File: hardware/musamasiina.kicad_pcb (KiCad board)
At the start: 2 copper layers, 50 x 45 mm, 73 parts, among them U2 MIC5233-3.3, U3 LTC6257, U4 TPS22860

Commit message: Start placement of parts
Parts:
- added C19: 470u, footprints:C_Radial_D6.3_L13_P2-5_Bent, F.Cu at (142.2, 56.5)
- added C20: 470u, footprints:C_Radial_D6.3_L13_P2-5_Bent, F.Cu at (142.2, 63.2)
- added C21: 470u, footprints:C_Radial_D6.3_L13_P2-5_Bent, F.Cu at (142.2, 70.0)
- added C4: AFK477M10F24T-F, footprints:C_Radial_D6.3_L13_P2-5_Bent, F.Cu at (142.2, 76.8)
- added P1: USB_OTG, Connect:USB_Micro-B_10103594-0001LF, F.Cu at (155.0, 90.0)
- added P2: CONN_02X05, Pin_Headers:Pin_Header_Straight_2x05_Pitch1.27mm, F.Cu at (131.2, 87.8)
- added P3: CONN_02X03, Pin_Headers:Pin_Header_Straight_2x03, F.Cu at (135.5, 98.0)
- added P4: CONN_01X06, Pin_Headers:Pin_Header_Straight_1x06, F.Cu at (145.0, 98.0)
- added U1: WT32, footprints:WT32, F.Cu at (123.0, 75.0)
- D1: footprint footprints:SMD0805-CAP-M -> footprints:SOD323-M
- U2: footprint footprints:SOT23-5-M -> footprints:SOT23-6-M
- U4: footprint footprints:SOT23-6-M -> footprints:SOT23-5-M
- moved D11 88.1 mm to (149.2, 58.0), turned to 180 degrees
- moved R23 87.1 mm to (149.2, 85.8), turned to 180 degrees
- moved R24 85.3 mm to (146.2, 79.6)
- moved FB11 85.3 mm to (156.0, 60.5)
- moved FB9 82.9 mm to (156.0, 57.0)
- moved FB2 82.8 mm to (149.2, 88.2), turned to 180 degrees
- moved C26 81.6 mm to (152.5, 58.0), turned to 270 degrees
- moved C27 79.5 mm to (152.5, 63.0), turned to 90 degrees
- moved FB10 79.1 mm to (156.0, 63.8)
- moved D12 78.4 mm to (149.2, 62.8)
- moved D5 72.5 mm to (145.5, 90.2), turned to 90 degrees
- moved R14 72.5 mm to (155.3, 115.4)
- moved D1 71.3 mm to (70.9, 139.2)
- moved FB1 67.8 mm to (149.2, 92.8), turned to 180 degrees
- moved C13 66.7 mm to (144.8, 94.5), turned to 180 degrees
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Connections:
- R6 pad 2: /USB_DN -> /USB_D-
- R7 pad 2: /USB_DP -> /USB_D+
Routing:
- net /USB_D-: track 0.00 -> 29.0 mm
- net /USB_D+: track 0.00 -> 28.3 mm
- net Net-(R7-Pad1): track 0.00 -> 3.17 mm
- net Net-(R6-Pad1): track 0.00 -> 3.17 mm
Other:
- board size 50 x 45 mm -> 50 x 50 mm
- net class Default: clearance 0.2 -> 0.15; via_dia 0.6 -> 0.7; via_drill 0.4 -> 0.3
- net class USB_DATA added: clearance 0.15, trace_width 0.225, via_dia 0.7, via_drill 0.3
- rule trace_clearance: 0.2 -> 0.15
- rule via_min_size: 0.4 -> 0.6

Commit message: Continue placing parts
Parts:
- added P5: CONN_01X03, footprints:SMD_3-5mm_jack_CUI-SJ-352X-SMT, B.Cu at (160.0, 59.0)
- added P6: CONN_01X03, footprints:SMD_3-5mm_jack_CUI-SJ-352X-SMT, B.Cu at (160.0, 69.2)
- added P7: CONN_01X03, footprints:SMD_3-5mm_jack_CUI-SJ-352X-SMT, B.Cu at (160.0, 79.5)
- C19, C20, C21, C4: moved to B.Cu
- moved C2 92.9 mm to (118.2, 48.5)
- moved C11 92.0 mm to (141.5, 88.5)
- moved C18 82.5 mm to (123.0, 53.0), turned to 180 degrees
- moved C14 81.7 mm to (117.2, 56.2), turned to 90 degrees
- moved R9 80.3 mm to (114.8, 56.2), turned to 270 degrees
- moved C16 77.0 mm to (125.2, 61.0)
- moved R16 76.7 mm to (133.8, 56.2), turned to 90 degrees
- moved R10 75.0 mm to (112.2, 56.2), turned to 90 degrees
- moved R15 73.0 mm to (131.2, 56.2), turned to 90 degrees
- moved R11 71.8 mm to (112.2, 60.8), turned to 270 degrees
- moved C15 71.7 mm to (120.8, 61.0)
- moved R21 70.8 mm to (128.8, 60.8), turned to 90 degrees
- moved R13 70.6 mm to (131.2, 60.8), turned to 270 degrees
- moved D4 70.4 mm to (123.9, 111.4)
- moved C3 70.3 mm to (123.0, 48.5)
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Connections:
- C7 pad 1: /Line in/ESD+ -> VAA
- C8 pad 1: /Line in/ESD+ -> VAA
- D10 pad 2: /Line in/ESD+ -> VAA
- D11 pad 2: /Line in/ESD+ -> VAA
- D12 pad 2: /Line in/ESD+ -> VAA
- D9 pad 2: /Line in/ESD+ -> VAA
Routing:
- net VCC: track 0.00 -> 1.50 mm, vias 0 -> 1
- net /IN_RIGHT: track 0.00 -> 1.50 mm, vias 0 -> 1
- net /IN_LEFT: track 0.00 -> 1.50 mm, vias 0 -> 1
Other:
- outline, holes or cut-outs redrawn

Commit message: Adjust layout
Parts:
- moved R18 58.8 mm to (107.4, 58.9)
- moved R19 43.1 mm to (136.2, 60.8), turned to 270 degrees
- moved P2 33.1 mm to (96.0, 78.0)
- moved R4 9.96 mm to (101.0, 84.0)
- moved D3 6.93 mm to (101.0, 86.0)
- moved FB1 2.26 mm to (149.5, 95.0)
- moved P1 2.00 mm to (155.0, 92.0)
- turned C15 to 180 degrees
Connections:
- net /Analog/N_LEFT renamed /Analog/LO_N
- net /Analog/N_RIGHT renamed /Analog/RO_N
- net /Analog/P_LEFT renamed /Analog/LO_P
- net /Analog/P_RIGHT renamed /Analog/RO_P
- net Net-(C15-Pad2) renamed /Analog/LEFT_OPAMP-
- net Net-(C16-Pad2) renamed /Analog/RIGHT_OPAMP-
- net Net-(R11-Pad1) renamed /Analog/LEFT_OPAMP+
- net Net-(R13-Pad1) renamed /Analog/RIGHT_OPAMP+
- net Net-(R6-Pad1) renamed /CD-
- net Net-(R7-Pad1) renamed /CD+
- C15 pad 1: Net-(C15-Pad1) -> /Analog/LEFT_SE
- C16 pad 1: Net-(C16-Pad1) -> /Analog/RIGHT_SE
- C19 pad 2: Net-(C15-Pad1) -> /Analog/LEFT_SE
- C20 pad 2: Net-(C16-Pad1) -> /Analog/RIGHT_SE
- R15 pad 2: /Stereo out/LEFT_DEVICE -> /Analog/LEFT_SE
- R16 pad 2: /Stereo out/RIGHT_DEVICE -> /Analog/RIGHT_SE
- R20 pad 1: Net-(C15-Pad1) -> /Analog/LEFT_SE
- R21 pad 1: Net-(C16-Pad1) -> /Analog/RIGHT_SE
- U3 pad 10: Net-(C16-Pad1) -> /Analog/RIGHT_SE
- U3 pad 7: Net-(C15-Pad1) -> /Analog/LEFT_SE
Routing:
- net /USB_D-: track 29.0 -> 0.00 mm
- net /USB_D+: track 28.3 -> 0.00 mm
- net /Analog/RO_P: track 0.00 -> 20.2 mm
- net /Analog/RO_N: track 0.00 -> 20.2 mm
- net /Analog/RIGHT_OPAMP-: track 0.00 -> 15.3 mm
- net /Analog/LEFT_OPAMP-: track 0.00 -> 14.1 mm
- net /Analog/LEFT_OPAMP+: track 0.00 -> 10.2 mm
- net /Analog/RIGHT_SE: track 0.00 -> 9.78 mm
- net /Analog/LEFT_SE: track 0.00 -> 9.77 mm
- net Net-(C14-Pad1): track 0.00 -> 9.43 mm
- net /Analog/RIGHT_OPAMP+: track 0.00 -> 7.57 mm
- net /Analog/LO_N: track 0.00 -> 6.50 mm
- net /Analog/LO_P: track 0.00 -> 5.93 mm
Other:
- net class Default: clearance 0.15 -> 0.2
- net class Opamp_differential added: clearance 0.15, trace_width 0.2, via_dia 0.7, via_drill 0.3
- rule trace_clearance: 0.15 -> 0.2

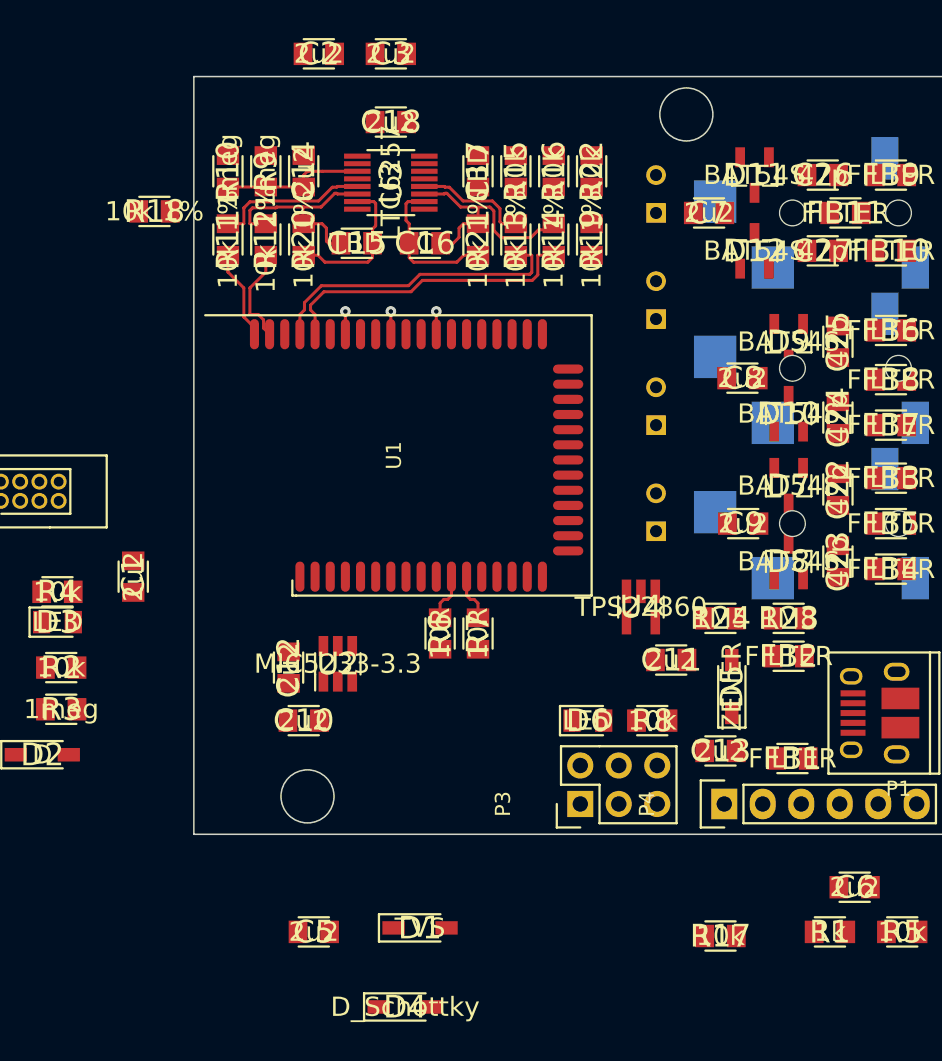
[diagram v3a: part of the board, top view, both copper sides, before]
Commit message: Add KiCAD footprints to project folder
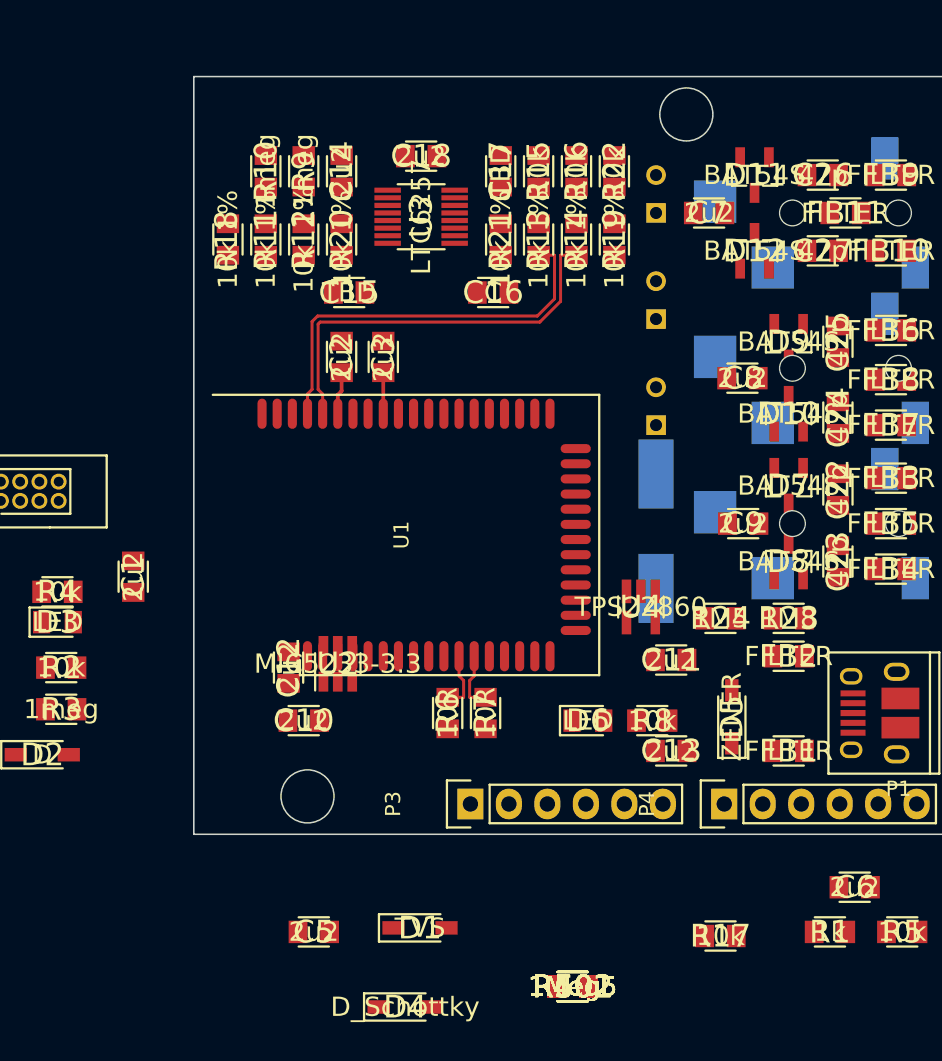
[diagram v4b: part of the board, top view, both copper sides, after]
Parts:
- added R401, R402, R501, R502, R601, R602: 1Meg5, footprints:SMD0805-RES-M, F.Cu at (135.0, 110.1)
- C4: footprint footprints:C_Radial_D6.3_L13_P2-5_Bent -> footprints:SMD_ELEC_8mmdia-M
- P3: footprint Pin_Headers:Pin_Header_Straight_2x03 -> kicad_lib:Pin_Header_Straight_1x06
- P4: footprint Pin_Headers:Pin_Header_Straight_1x06 -> kicad_lib:Pin_Header_Straight_1x06
- moved C2 20.1 mm to (119.8, 68.5), turned to 270 degrees
- moved C3 20.0 mm to (122.5, 68.5), turned to 270 degrees
- moved P3 7.25 mm to (128.2, 98.0)
- moved C16 5.55 mm to (129.8, 64.2), turned to 180 degrees
- moved R6 5.27 mm to (126.8, 92.0)
- moved R7 5.27 mm to (129.2, 92.0)
- moved U1 5.27 mm to (123.5, 80.2)
- moved R18 5.19 mm to (112.2, 60.8), turned to 270 degrees
- moved C15 3.29 mm to (120.2, 64.2), turned to 0 degrees
- moved C13 3.25 mm to (141.5, 94.5)
- moved C18 3.01 mm to (125.0, 55.2)
- moved U3 3.01 mm to (125.0, 59.2)
- moved C14 2.50 mm to (119.8, 56.2)
- moved R10 2.50 mm to (114.8, 56.2)
- moved R11 2.50 mm to (114.8, 60.8)
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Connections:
- P1 pad 4: Net-(P1-Pad4) -> /Power Supply/GNDBUS
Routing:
- net /Analog/RIGHT_OPAMP-: track 15.3 -> 0.00 mm
- net /Analog/LEFT_OPAMP-: track 14.1 -> 0.00 mm
- net /Analog/LEFT_OPAMP+: track 10.2 -> 0.00 mm
- net /Analog/RIGHT_SE: track 9.78 -> 0.00 mm
- net /Analog/LEFT_SE: track 9.77 -> 0.00 mm
- net Net-(C14-Pad1): track 9.43 -> 0.00 mm
- net /Analog/RIGHT_OPAMP+: track 7.57 -> 0.00 mm
- net /Analog/RO_N: track 20.2 -> 26.8 mm
- net /Analog/RO_P: track 20.2 -> 26.8 mm
- net /Analog/LO_N: track 6.50 -> 0.00 mm
- net /Analog/LO_P: track 5.93 -> 0.00 mm
- net Net-(C2-Pad2): track 0.00 -> 2.81 mm
- net Net-(C3-Pad2): track 0.00 -> 2.71 mm
- net VCC: track 1.50 -> 0.00 mm, vias 1 -> 0
- net /IN_RIGHT: track 1.50 -> 0.00 mm, vias 1 -> 0
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
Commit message: Update layout
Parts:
- removed R401, R402, R501, R502, R601, R602: 1Meg5, footprints:SMD0805-RES-M
- added C28: 2u2, footprints:SMD0805-CAP-M, F.Cu at (142.8, 82.8)
- added R25: 1Meg5, footprints:SMD0805-RES-M, F.Cu at (143.8, 76.0)
- added R26: 1Meg5, footprints:SMD0805-RES-M, F.Cu at (151.5, 74.2)
- added R27: 1Meg5, footprints:SMD0805-RES-M, F.Cu at (151.5, 64.0)
- added R28: 1Meg5, footprints:SMD0805-RES-M, F.Cu at (156.0, 74.2)
- added R29: 1Meg5, footprints:SMD0805-RES-M, F.Cu at (156.0, 64.0)
- added R30: 1Meg5, footprints:SMD0805-RES-M, F.Cu at (143.0, 62.5)
- C4: footprint footprints:SMD_ELEC_8mmdia-M -> footprints:C_Radial_D6.3_L13_P2-5_Bent
- P2: moved to B.Cu
- P4: footprint kicad_lib:Pin_Header_Straight_1x06 -> Pin_Headers:Pin_Header_Straight_1x06
- moved R17 54.5 mm to (126.7, 55.2)
- moved R1 44.4 mm to (132.5, 66.5)
- moved C6 43.7 mm to (127.5, 68.5), turned to 270 degrees
- moved D2 42.8 mm to (137.2, 73.8), turned to 270 degrees
- moved R2 40.6 mm to (136.0, 68.0), turned to 90 degrees
- moved C5 38.6 mm to (125.0, 68.5), turned to 270 degrees
- moved D1 37.6 mm to (131.8, 69.2)
- moved D4 34.3 mm to (137.2, 79.8), turned to 90 degrees
- moved R4 24.2 mm to (123.2, 93.5)
- moved D3 22.8 mm to (123.2, 91.0)
- moved R5 21.2 mm to (142.0, 91.2), turned to 180 degrees
- moved C10 21.0 mm to (138.2, 92.2), turned to 270 degrees
- moved R3 18.5 mm to (119.8, 92.0), turned to 270 degrees
- moved P2 18.5 mm to (112.2, 69.2), turned to 0 degrees
- moved U2 15.9 mm to (135.0, 92.2), turned to 180 degrees
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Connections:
- C11 pad 2: GNDA -> GNDD
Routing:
- net /USB_D+: track 0.00 -> 30.9 mm
- net /USB_D-: track 0.00 -> 30.9 mm
- net /Analog/LEFT_OPAMP-: track 0.00 -> 15.8 mm
- net /Analog/RIGHT_OPAMP+: track 0.00 -> 14.2 mm
- net Net-(C14-Pad1): track 0.00 -> 13.3 mm
- net /Analog/LO_P: track 0.00 -> 13.2 mm
- net /Analog/LO_N: track 0.00 -> 13.0 mm
- net /Analog/RIGHT_OPAMP-: track 0.00 -> 12.5 mm
- net /Analog/LEFT_OPAMP+: track 0.00 -> 9.48 mm
- net /Analog/LEFT_SE: track 0.00 -> 6.47 mm
- net VAA: track 0.00 -> 4.43 mm
- net /Analog/RIGHT_SE: track 0.00 -> 4.00 mm
- net /PLAY: track 0.00 -> 2.83 mm
- net Net-(C2-Pad2): track 2.81 -> 0.00 mm
- net Net-(C3-Pad2): track 2.71 -> 0.00 mm
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
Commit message: Layout board
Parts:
- removed C14, C18, C8, C9: 2u2, footprints:SMD0805-CAP-M
- removed C15, C17: TBD, footprints:SMD0805-CAP-M
- removed C16: C, footprints:SMD0805-CAP-M
- removed C19, C20, C21: 470u, footprints:C_Radial_D6.3_L13_P2-5_Bent
- removed C22, C23, C24, C25: 47p, footprints:SMD0805-CAP-M
- removed D10, D11, D12, D7, D8, D9: BAT54S, footprints:SOT23-M
- removed D2: D, footprints:SOD323-M
- removed D3, D6: LED, footprints:SMD0805-LED-M
- removed D4: D_Schottky, footprints:SOD323-M
- removed D5: ZENER, footprints:SOD323-M
- removed FB3, FB4, FB5, FB6, FB7, FB8: FILTER, footprints:SMD0805-FERRITE-M
- removed P5, P6, P7: CONN_01X03, footprints:SMD_3-5mm_jack_CUI-SJ-352X-SMT
- removed R14, R18, R19, R20, R21: 10k 1%, footprints:SMD0805-RES-M
- removed R15, R16, R17, R22: 10k, footprints:SMD0805-RES-M
- removed R23: 1M8, footprints:SMD0805-RES-M
- removed R24: 1M5, footprints:SMD0805-RES-M
- removed R25, R26, R27, R28: 1Meg5, footprints:SMD0805-RES-M
- added BT1: Battery, Pin_Headers:Pin_Header_Angled_1x02, B.Cu at (130.0, 51.7)
- added Q1: Q_NMOS_DGS, footprints:SOT23-M, F.Cu at (118.2, 85.8)
- added REF**: BREAKAWAY_5, BREAKAWAY_5, F.Cu at (136.2, 53.0)
- added REF**: BREAKAWAY_5, BREAKAWAY_5, F.Cu at (136.2, 85.2)
- added U5: CD143A-SR05, footprints:SOT143-N, F.Cu at (127.8, 60.8)
- added U6: LM2776, footprints:SOT23-6-M, F.Cu at (121.7, 53.7)
- added U7: CD143A-SR05, footprints:SOT143-N, F.Cu at (112.2, 61.5)
- C1, C10, C11, C12, C13, C2, C26, C27, C28, C3, C6, C7: footprint footprints:SMD0805-CAP-M -> footprints:SMD0402-CAP-N
- C4: value AFK477M10F24T-F -> 47p; footprint footprints:C_Radial_D6.3_L13_P2-5_Bent -> footprints:SMD0402-CAP-N; moved to F.Cu
- C5: value 2u2 -> 47p; footprint footprints:SMD0805-CAP-M -> footprints:SMD0402-CAP-N
- D1: value TVS -> D_Schottky
- FB1, FB10, FB11, FB2, FB9: footprint footprints:SMD0805-FERRITE-M -> footprints:SMD0402-FERRITE-N
- P2: value CONN_02X05 -> CONN_01X04; footprint Pin_Headers:Pin_Header_Straight_2x05_Pitch1.27mm -> footprints:SMD_3-5mm_jack_CUI-SJ-352X-SMT
- R1, R4, R5, R6, R7, R8: footprint footprints:SMD0805-RES-M -> footprints:SMD0402-RES-N
- R10, R3, R9: value 1meg -> 10k; footprint footprints:SMD0805-RES-M -> footprints:SMD0402-RES-N
- R11, R12, R13: value 10k 1% -> 10k; footprint footprints:SMD0805-RES-M -> footprints:SMD0402-RES-N
- R2: value 10k -> 1meg; footprint footprints:SMD0805-RES-M -> footprints:SMD0402-RES-N
- R29, R30: value 1Meg5 -> 10k; footprint footprints:SMD0805-RES-M -> footprints:SMD0402-RES-N
- U3: value LTC6257 -> LT6221; footprint footprints:MSOP16-05mm-M -> footprints:DFN-8-EP-0_5mm_3x3mm-N
- U4: footprint footprints:SOT23-5-M -> footprints:SOT23-6-M
- moved P3 45.6 mm to (139.7, 55.9), turned to 0 degrees
- moved FB9 44.0 mm to (112.0, 57.7), turned to 90 degrees
- moved R8 42.5 mm to (115.2, 62.8), turned to 270 degrees
- moved C26 40.8 mm to (110.8, 57.8), turned to 90 degrees
- moved FB10 40.8 mm to (115.2, 61.2), turned to 180 degrees
- moved R4 39.8 mm to (116.5, 54.2), turned to 90 degrees
- moved FB2 39.6 mm to (128.5, 57.2)
- moved P1 39.5 mm to (133.0, 59.8)
- moved C28 38.3 mm to (121.8, 50.8), turned to 180 degrees
- moved R3 38.0 mm to (115.2, 54.2), turned to 90 degrees
- moved C13 37.8 mm to (125.2, 60.8), turned to 270 degrees
- moved FB1 37.5 mm to (128.5, 63.2)
- moved C11 36.8 mm to (125.0, 54.8)
- moved U4 35.6 mm to (126.1, 52.0), turned to 270 degrees
- moved R29 34.8 mm to (121.2, 62.8)
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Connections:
- C1 pad 1: Net-(C1-Pad1) -> VAA
- C1 pad 2: GNDD -> GNDA
- C2 pad 1: GNDA -> VEE
- C2 pad 2: Net-(C2-Pad2) -> GNDA
- C3 pad 1: GNDA -> VAA
- C3 pad 2: Net-(C3-Pad2) -> VEE
- C4 pad 1: +BATT -> /Stereo out/LEFT_DEVICE
- C4 pad 2: GNDD -> Net-(C4-Pad2)
- C5 pad 1: /Line in/LEFT_DEVICE -> /Stereo out/RIGHT_DEVICE
- C5 pad 2: /IN_LEFT -> Net-(C5-Pad2)
- C6 pad 1: /Line in/RIGHT_DEVICE -> Net-(C6-Pad1)
- C6 pad 2: /IN_RIGHT -> Net-(C6-Pad2)
- C7 pad 1: VAA -> VEE
- D1 pad 1: +BATT -> +5V
- D1 pad 2: Net-(D1-Pad2) -> +BATT
- P2 pad 1: VDD -> /Stereo out/LEFT_CABLE
- P2 pad 2: /PREV -> /Stereo out/GROUND_CABLE
- P2 pad 3: /VOL- -> /Stereo out/RIGHT_CABLE
- P2 pad 4: /NEXT -> /AUDIO_SWITCH
- P3 pad 2: VDD -> +5V
- P4 pad 3: VDD -> +5V
- R1 pad 1: Net-(C1-Pad1) -> /Power Supply/ENABLE
- R1 pad 2: Net-(D1-Pad2) -> Net-(Q1-Pad3)
- R10 pad 1: Net-(C14-Pad1) -> Net-(C5-Pad2)
- R10 pad 2: GNDA -> /RO_N
- R11 pad 1: /Analog/LEFT_OPAMP+ -> /Stereo out/LEFT_DEVICE
- R11 pad 2: /Analog/LO_P -> Net-(C4-Pad2)
- R12 pad 1: /Analog/LEFT_OPAMP- -> /Stereo out/RIGHT_DEVICE
- R12 pad 2: /Analog/LO_N -> Net-(C5-Pad2)
- R13 pad 1: /Analog/RIGHT_OPAMP+ -> Net-(C4-Pad2)
- R13 pad 2: /Analog/RO_P -> /LO_N
- R2 pad 1: Net-(D3-Pad2) -> +BATT
- R2 pad 2: /Power Supply/ENABLE -> /AUDIO_SWITCH
- R3 pad 1: Net-(D3-Pad2) -> Net-(R3-Pad1)
- R3 pad 2: GNDD -> GNDA
- R4 pad 1: Net-(D3-Pad1) -> Net-(R3-Pad1)
- R4 pad 2: GNDD -> /LO_P
- R8 pad 1: +5V -> Net-(R8-Pad1)
- R8 pad 2: Net-(D6-Pad2) -> GNDA
- R9 pad 1: VAA -> Net-(R8-Pad1)
- R9 pad 2: Net-(C14-Pad1) -> /RO_P
- U1 pad 1: Net-(C1-Pad1) -> /Power Supply/ENABLE
- U1 pad 36: /Power Supply/CHRG -> /CHRG
- U1 pad 38: VCC -> +5V
- U1 pad 42: Net-(C3-Pad2) -> Net-(U1-Pad42)
- U1 pad 45: Net-(C2-Pad2) -> Net-(U1-Pad45)
- U1 pad 46: /Analog/RO_N -> /RO_N
- U1 pad 47: /Analog/RO_P -> /RO_P
- U1 pad 49: /Analog/LO_N -> /LO_N
- U1 pad 50: /Analog/LO_P -> /LO_P
- U1 pad 7: Net-(D3-Pad2) -> Net-(U1-Pad7)
- U3 pad 1: VCOM -> /Stereo out/LEFT_DEVICE
- U3 pad 2: VCOM -> Net-(C4-Pad2)
- U3 pad 3: Net-(C14-Pad1) -> Net-(R3-Pad1)
- U3 pad 4: VAA -> VEE
- U3 pad 5: /Analog/LEFT_OPAMP+ -> Net-(R8-Pad1)
- U3 pad 6: /Analog/LEFT_OPAMP- -> Net-(C5-Pad2)
- U3 pad 7: /Analog/LEFT_SE -> /Stereo out/RIGHT_DEVICE
- U3 pad 8: (no net) -> VAA
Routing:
- net +5V: track 0.00 -> 106.5 mm, vias 0 -> 4
- net GNDD: track 0.00 -> 82.6 mm, vias 0 -> 10
- net +BATT: track 0.00 -> 64.1 mm, vias 0 -> 4
- net /Power Supply/ENABLE: track 0.00 -> 49.7 mm, vias 0 -> 2
- net /RESET: track 0.00 -> 41.4 mm, vias 0 -> 2
- net VAA: track 4.43 -> 40.8 mm, vias 0 -> 2
- net /AUDIO_SWITCH: track 0.00 -> 34.5 mm, vias 0 -> 1
- net /MOSI: track 0.00 -> 33.0 mm, vias 0 -> 1
- net /RXD: track 0.00 -> 28.8 mm, vias 0 -> 1
- net /Analog/RO_P: track 27.7 -> 0.00 mm
- net /Analog/RO_N: track 27.7 -> 0.00 mm
- net /SCLK: track 0.00 -> 26.7 mm, vias 0 -> 2
- net /MISO: track 0.00 -> 25.4 mm
- net /Stereo out/LEFT_DEVICE: track 0.00 -> 24.1 mm
- net /TXD: track 0.00 -> 22.7 mm, vias 0 -> 2
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- added copper zone on In1.Cu, net GNDA
- added copper zone on In1.Cu, net GNDD
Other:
- board size 50 x 50 mm -> 32.5 x 40 mm
- copper layers 2 -> 4
- net class Default: clearance 0.2 -> 0.17
- net class Opamp_differential: clearance 0.15 -> 0.17
- net class USB_DATA: clearance 0.15 -> 0.17
- rule trace_clearance: 0.2 -> 0.17
- rule trace_min: 0.2 -> 0.18
- board text added: "BATTERY"
- board text added: "otso@ojousima.net"
- board text added: "poppimASiina TINY"

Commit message: Add production files, printouts
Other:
- board text added: "poppimASiina TINY 2016-06-05"
- board text added: "rev. 2ac7968"
- board text removed: "poppimASiina TINY"
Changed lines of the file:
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@@
     (area 109.949999 49.949999 142.550001 90.050001)
     (thickness 1.6)
-    (drawings 56)
+    (drawings 59)
     (tracks 808)
     (zones 0)
@@
   (page A4)
   (layers
-    (0 F.Cu signal)
+    (0 F.Cu signal hide)
     (1 In1.Cu power hide)
     (2 In2.Cu power hide)
@@
     (pad_to_mask_clearance 0)
     (aux_axis_origin 0 0)
-    (visible_elements 7FFCFFFF)
+    (visible_elements 7FFEBDFF)
     (pcbplotparams
-      (layerselection 0x00030_80000001)
-      (usegerberextensions false)
-      (excludeedgelayer true)
+      (layerselection 0x010f0_80000007)
+      (usegerberextensions true)
+      (excludeedgelayer false)
       (linewidth 0.100000)
       (plotframeref false)
@@
       (psnegative false)
       (psa4output false)
-      (plotreference true)
-      (plotvalue true)
+      (plotreference false)
+      (plotvalue false)
       (plotinvisibletext false)
       (padsonsilk false)
@@
       (outputformat 1)
       (mirror false)
-      (drillshape 1)
+      (drillshape 0)
       (scaleselection 1)
-      (outputdirectory ""))
+      (outputdirectory gerber/))
   )
   (net 0 "")
@@
     (descr "Through hole pin header")
     (tags "pin header")
-    (fp_text reference BT1 (at 0 5.1 270) (layer B.SilkS)
+    (fp_text reference BT1 (at 0 -4.6 270) (layer B.SilkS)
       (effects (font (size 1 1) (thickness 0.15)) (justify mirror))
     )
@@
     )
   )
+  (gr_line (start 127.5 52.2) (end 127.5 51.1) (angle 90) (layer B.SilkS) (width 0.1))
+  (gr_line (start 126.9 51.6) (end 128 51.6) (angle 90) (layer B.SilkS) (width 0.1))
+  (gr_text "rev. 2ac7968" (at 117.7 51.7 180) (layer B.SilkS)
+    (effects (font (size 1.5 1.5) (thickness 0.3)) (justify mirror))
+  )
   (gr_text BATTERY (at 125.8 77.5 90) (layer B.SilkS)
     (effects (font (size 4 4) (thickness 0.3)) (justify mirror))
   )
-  (gr_text "poppimASiina TINY" (at 111 66 90) (layer B.SilkS)
+  (gr_text "poppimASiina TINY 2016-06-05" (at 111.75 64.5 90) (layer B.SilkS)
     (effects (font (size 1 1) (thickness 0.2)) (justify left mirror))
   )
